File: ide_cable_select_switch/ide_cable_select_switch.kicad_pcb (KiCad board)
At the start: 2 copper layers, 23.9 x 56.5 mm, 4 parts, among them J1 Conn_02x20_Odd_Even, J2 Conn_02x20_Odd_Even, J3 Conn_02x20_Odd_Even, SW1 SW_SPDT

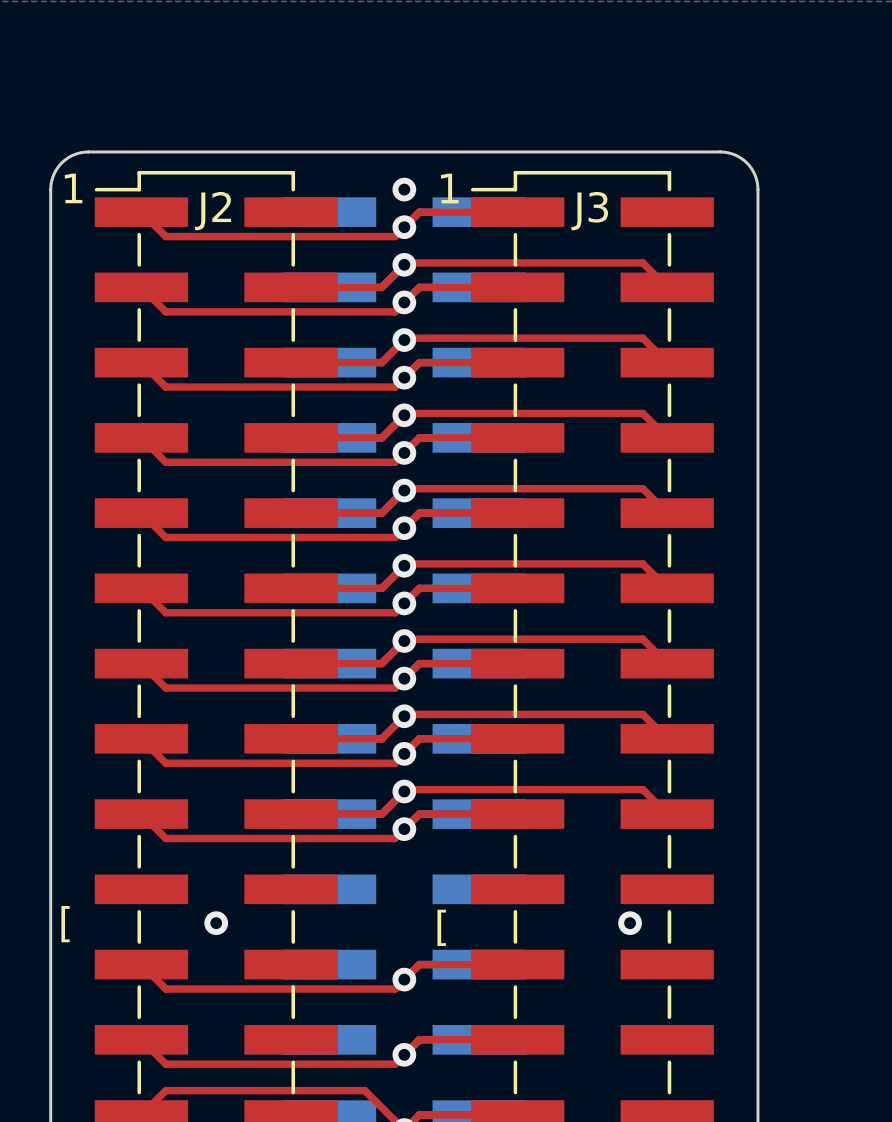
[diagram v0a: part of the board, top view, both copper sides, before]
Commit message: Move ground vias now that key pins are not in the way
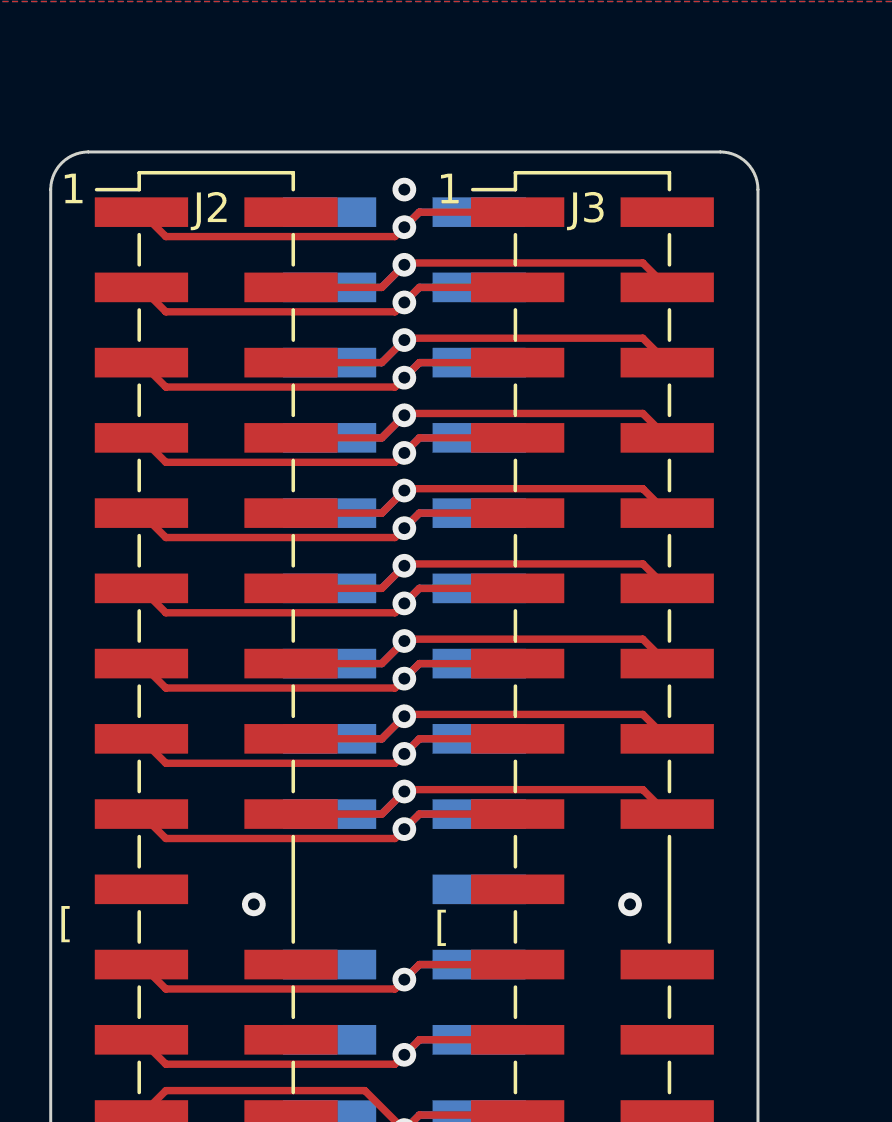
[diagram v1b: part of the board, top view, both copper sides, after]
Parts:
- J1, J2, J3: footprint Connector_PinHeader_2.54mm:PinHeader_2x20_P2.54mm_Vertical_SMD -> ide_cable_select_switch:IDE_ATA_Male_2x20_P2.54mm_Vertical_SMD

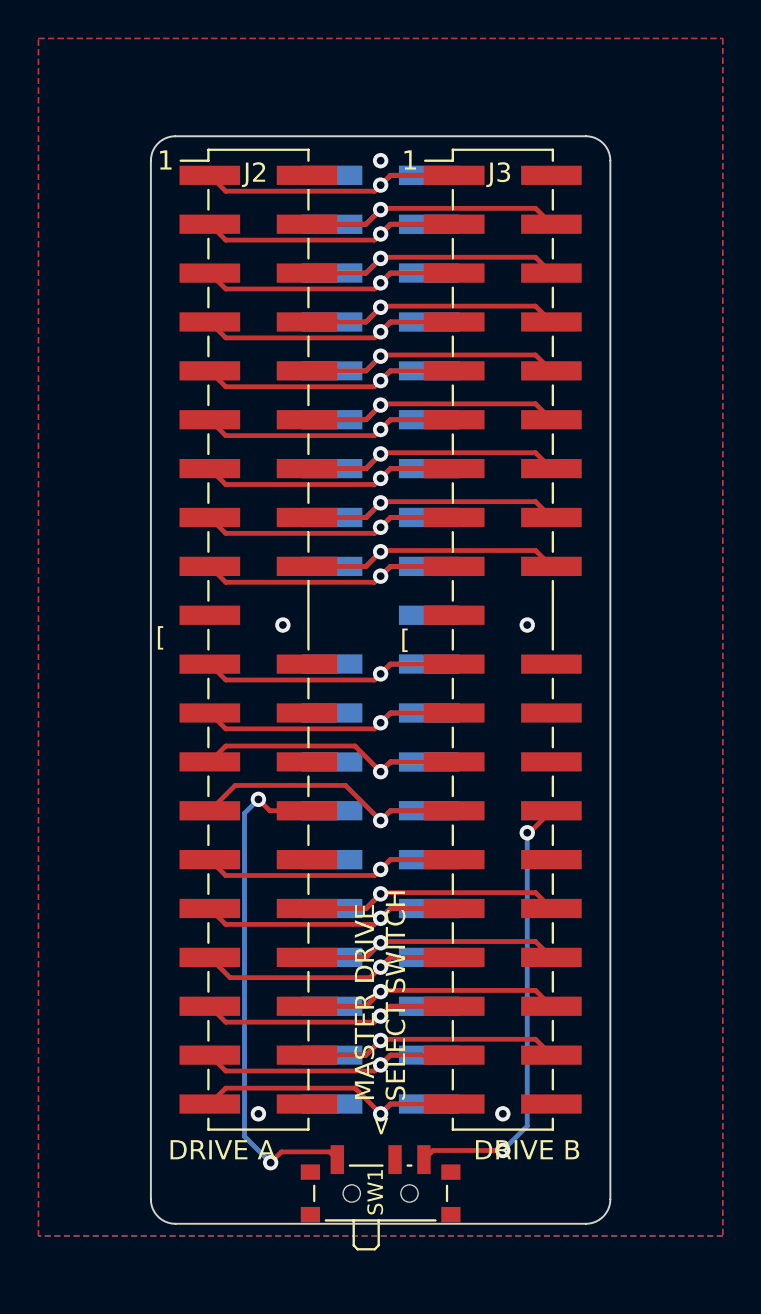
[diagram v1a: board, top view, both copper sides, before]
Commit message: Extend PCB below switch to help with unplugging leverage
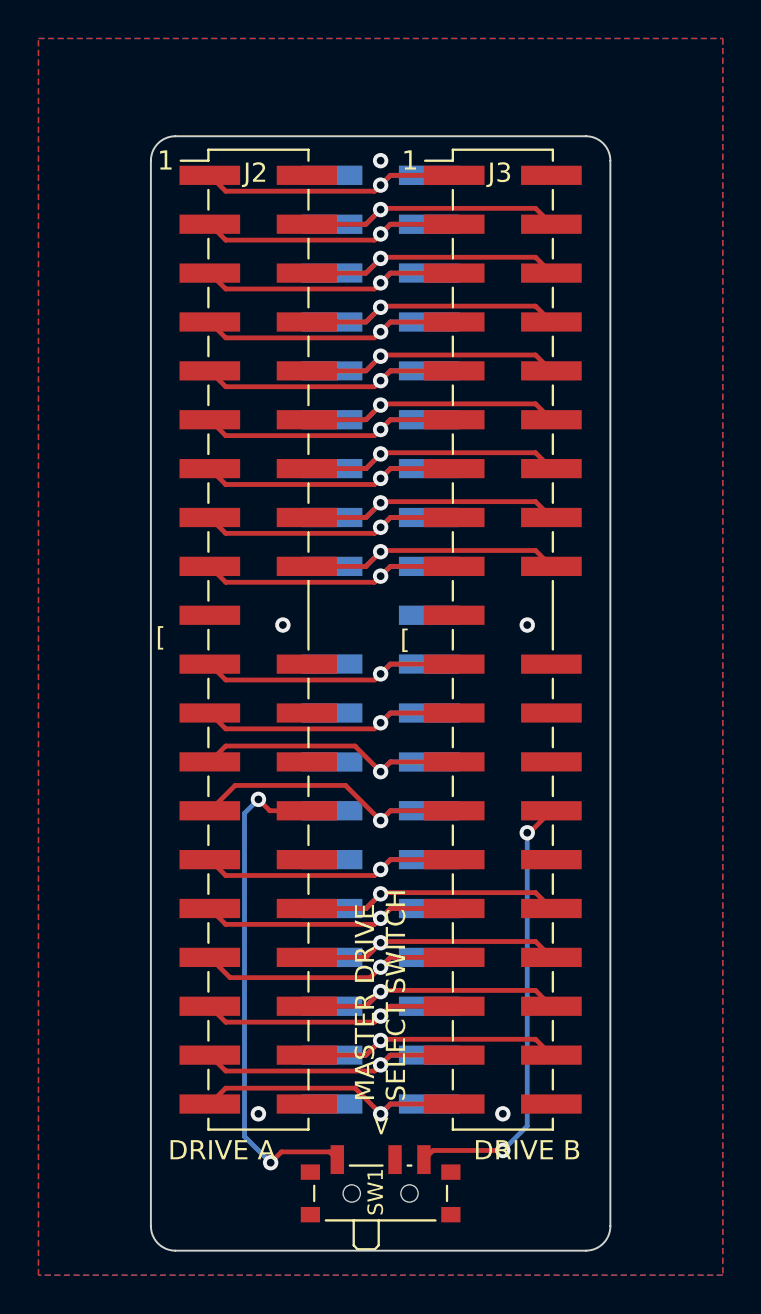
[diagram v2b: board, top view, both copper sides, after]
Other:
- board size 23.9 x 56.5 mm -> 23.9 x 57.9 mm
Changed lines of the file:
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@@
     )
   )
-  (gr_line (start 166.877999 113.664999) (end 166.878 59.69) (layer "Edge.Cuts") (width 0.1))
+  (gr_line (start 166.878 115.062) (end 166.878 59.69) (layer "Edge.Cuts") (width 0.1))
   (gr_line (start 165.608 58.42) (end 144.272 58.42) (layer "Edge.Cuts") (width 0.1))
-  (gr_line (start 144.272 114.934999) (end 165.607999 114.934999) (layer "Edge.Cuts") (width 0.1))
-  (gr_arc (start 144.272 114.934999) (mid 143.373974 114.563025) (end 143.002 113.664999) (layer "Edge.Cuts") (width 0.1))
-  (gr_arc (start 166.877999 113.664999) (mid 166.506025 114.563025) (end 165.607999 114.934999) (layer "Edge.Cuts") (width 0.1))
+  (gr_line (start 144.272001 116.332) (end 165.608 116.332) (layer "Edge.Cuts") (width 0.1))
+  (gr_arc (start 144.272001 116.332) (mid 143.373976 115.960026) (end 143.002001 115.062) (layer "Edge.Cuts") (width 0.1))
+  (gr_arc (start 166.878 115.062) (mid 166.506026 115.960026) (end 165.608 116.332) (layer "Edge.Cuts") (width 0.1))
   (gr_arc (start 165.608 58.42) (mid 166.506026 58.791974) (end 166.878 59.69) (layer "Edge.Cuts") (width 0.1))
   (gr_arc (start 143.002 59.69) (mid 143.373974 58.791974) (end 144.272 58.42) (layer "Edge.Cuts") (width 0.1))
-  (gr_line (start 143.002 59.69) (end 143.002 113.664999) (layer "Edge.Cuts") (width 0.1))
+  (gr_line (start 143.002 59.69) (end 143.002001 115.062) (layer "Edge.Cuts") (width 0.1))
   (gr_text "[" (at 160.02 84.582) (layer "B.SilkS")
     (effects (font (size 1 1) (thickness 0.15)) (justify mirror))
@@
     (polygon
       (pts
-        (xy 172.72 115.57)
-        (xy 137.16 115.57)
+        (xy 172.72 117.602)
+        (xy 137.16 117.602)
         (xy 137.16 53.34)
         (xy 172.72 53.34)

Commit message: Added IDC key indicator to sinkscreen
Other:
- board text added: "Change Master Drive Select Switch ONLY while system power is OFF"
- board text added: "Set both connected drives to {dblquote}Cable Select{dblquote} jumper setting"
- board text removed: "KEY"
- board text removed: "ONLY change Master Drive Select Switch while system power is OFF"
- board text removed: "Set both connected drives to {dblquote}CS{dblquote} or {dblquote}CSEL{dblquote} jumper setting"

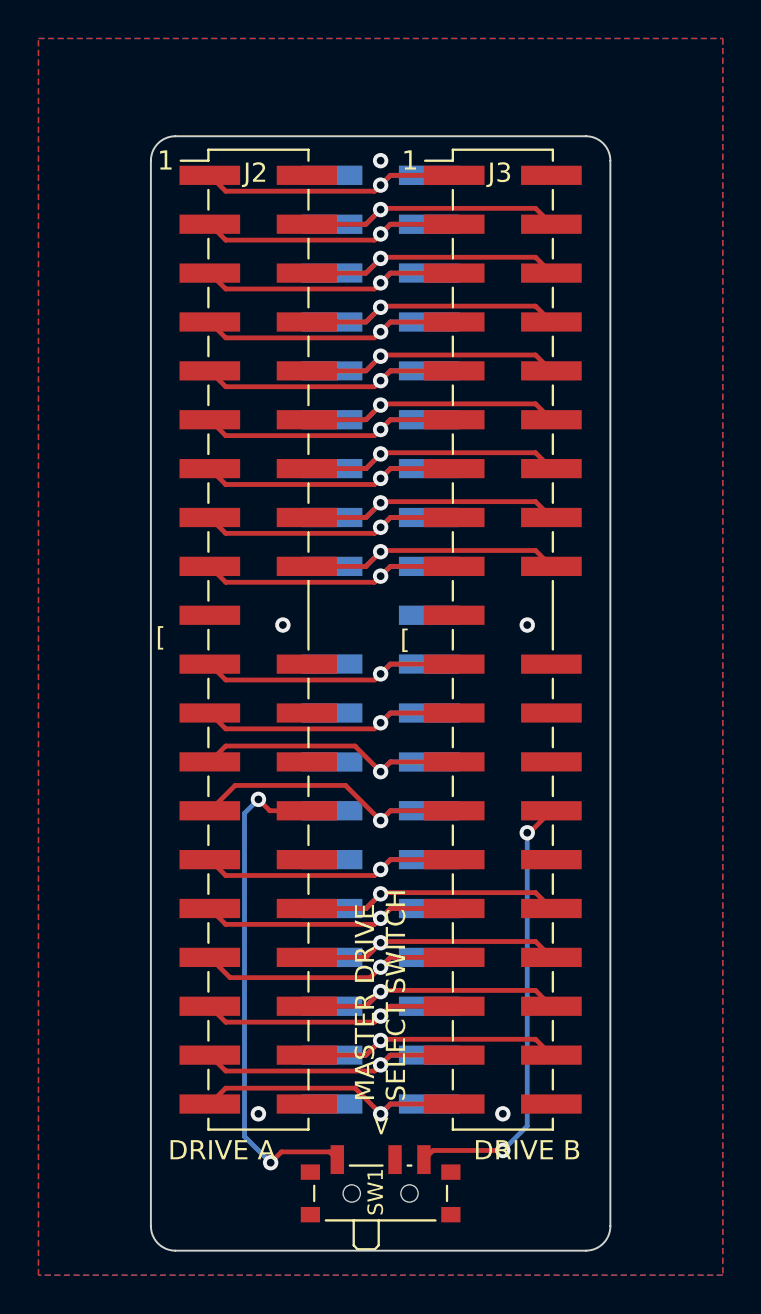
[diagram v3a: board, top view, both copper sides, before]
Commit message: Add pads for external switch
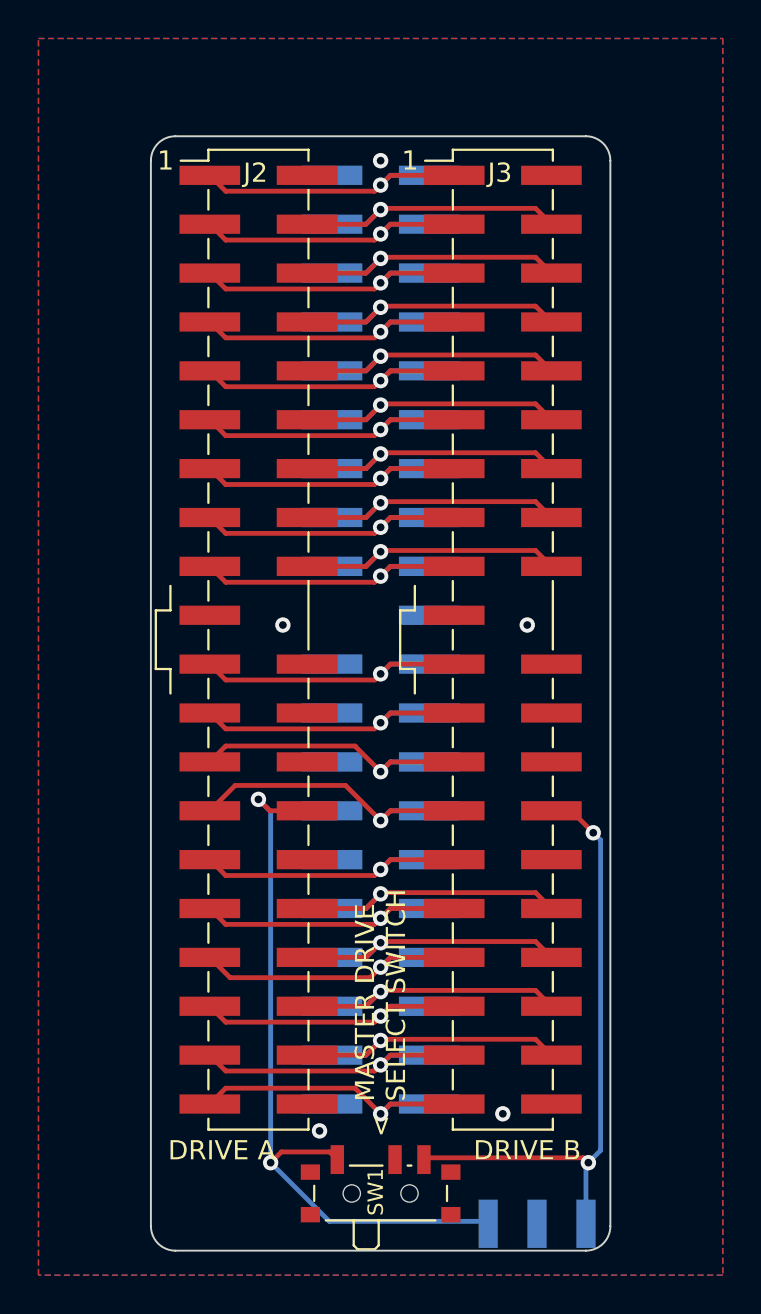
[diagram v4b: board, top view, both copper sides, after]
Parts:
- added J4: Conn_01x03_Male, ide_cable_select_switch:PinHeader_1x03_P2.54mm_Edge_SMD, B.Cu at (163.1, 114.9)
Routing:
- net CSEL_OUT_A: track 26.4 -> 38.3 mm
- net CSEL_OUT_B: track 23.1 -> 32.0 mm
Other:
- board text added: "< For Remote Switch"
- board text added: "Drive A"
- board text added: "Drive B"
- board text added: "GND"
- board text removed: "["

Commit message: Remove extra switch pads; turn main switch in to 2.54 header so it can be used for both a fixed and remote switch using the same footprint.
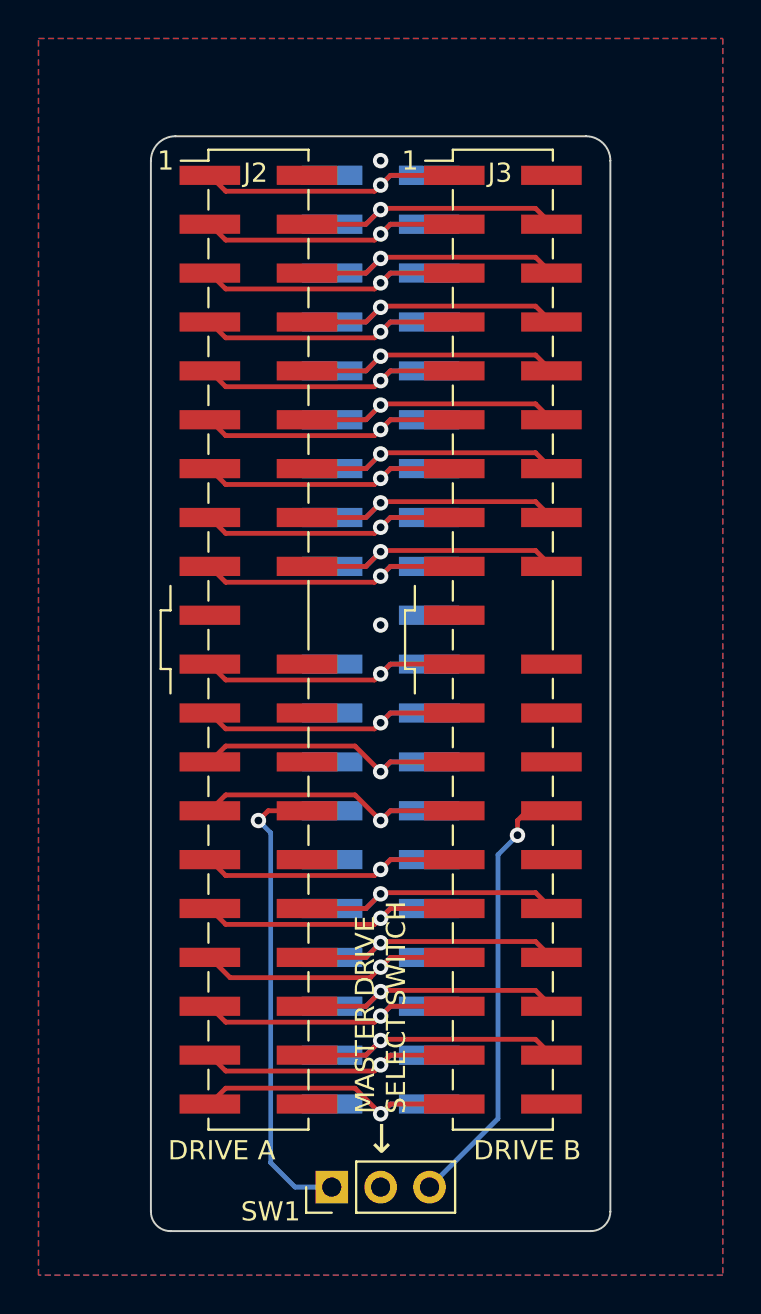
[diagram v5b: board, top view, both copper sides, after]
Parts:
- removed J4: Conn_01x03_Male, ide_cable_select_switch:PinHeader_1x03_P2.54mm_Edge_SMD
- SW1: footprint Button_Switch_SMD:SW_SPDT_PCM12 -> Connector_PinHeader_2.54mm:PinHeader_1x03_P2.54mm_Vertical
- moved SW1 2.54 mm to (152.4, 113.0), turned to 90 degrees
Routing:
- net CSEL_OUT_A: track 38.3 -> 24.5 mm, vias 2 -> 1
- net CSEL_OUT_B: track 32.0 -> 22.9 mm, vias 2 -> 1
- net GND: vias 5 -> 2
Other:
- board size 23.9 x 57.9 mm -> 23.9 x 56.9 mm
- board text added: "github.com/xunker ©2022 CC NC-BY-SA 4.0"
- board text added: "‼"
- board text added: "←"
- board text added: "↑ TO IDE CONTROLLER ↑"
- board text removed: "<"
- board text removed: "< For Remote Switch"
- board text removed: "Drive A"
- board text removed: "Drive B"
- board text removed: "GND"
- board text removed: "HOST IDE"
- board text removed: "github.com/xunker (C) 2022 CC NC-BY-SA 4.0"
